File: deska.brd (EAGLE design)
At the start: 72.1 x 55.9 mm, 19 parts, among them Q1 BC547, X1 JST-XH-03-PIN-LONG-PAD, X2 JST-XH-03-PIN-LONG-PAD, X3 JST-XH-03-PIN-LONG-PAD, X4 JST-XH-04-PIN-LONG-PAD, X5 JST-XH-04-PIN-LONG-PAD, X6 JST-XH-04-PIN-LONG-PAD

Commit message: deska
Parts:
- added LED2: (no value), led:LED3MM
- added R7: 220, rcl:0207/7
- moved R5 4.02 mm to (48.3, 34.3), turned to 180 degrees
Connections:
- removed net N$9: WEMOS1.GND, X4.3, X5.3, X6.3
- new net N$4: LED2.A, R7.2
- net +5V: now also R7.1
- net GND: now also LED2.K, WEMOS1.GND, X4.3, X5.3, X6.3
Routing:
- net +5V: track 77.2 -> 138.2 mm
- net N$9: track 25.4 -> 0.00 mm
- net GND: track 166.1 -> 187.7 mm
- net N$4: track 0.00 -> 7.93 mm
- net N$2: track 40.5 -> 43.8 mm
- net N$14: track 29.3 -> 26.7 mm
- net N$7: track 26.9 -> 29.0 mm

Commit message: 0.93
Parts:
- added X7: JST-XH-03-PIN-LONG-PAD, Rembrandt Electronics - JST XH Connectors v1-0:JST-XH-03-PACKAGE-LONG-PAD
- LED2: value (none) -> LED2
- NAPAJENI: value (none) -> 5V
- WEMOS1: value (none) -> WEMOS
- moved R4 10.9 mm to (48.3, 31.8), turned to 180 degrees
- moved R6 10.2 mm to (39.4, 45.7)
- moved LED1 6.35 mm to (35.6, 14.0), turned to 270 degrees
- moved LEDRELAY 6.35 mm to (29.2, 14.0), turned to 270 degrees
- moved R5 2.54 mm to (45.7, 34.3)
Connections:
- removed net N$5: R4.1, WEMOS1.D8
- new net N$9: R3.1, WEMOS1.D7, X3.1
- net +3V3: now also X7.2
- net BUILTINLED: now also R4.1
- net GND: now also X7.1
- net N$1: now also WEMOS1.D5; no longer WEMOS1.D0
- net N$19: now also WEMOS1.D6; no longer WEMOS1.D5
- net N$3: now also WEMOS1.D8, X7.3; no longer R3.1, WEMOS1.D6, X3.1
- net N$8: now also WEMOS1.D0; no longer WEMOS1.D7
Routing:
- net GND: track 187.7 -> 226.2 mm
- net N$2: track 43.8 -> 25.8 mm
- net N$9: track 0.00 -> 14.3 mm
- net +3V3: track 76.6 -> 85.5 mm
- net +5V: track 138.2 -> 130.5 mm
- net N$3: track 16.8 -> 24.0 mm
- net N$7: track 29.0 -> 23.3 mm
- net N$5: track 5.08 -> 0.00 mm
- net BUILTINLED: track 0.00 -> 5.08 mm
- net N$14: track 26.7 -> 30.8 mm
- net N$6: track 16.8 -> 20.2 mm
- net N$8: track 5.08 -> 6.13 mm
- net N$1: track 13.2 -> 14.3 mm, vias 1 -> 0

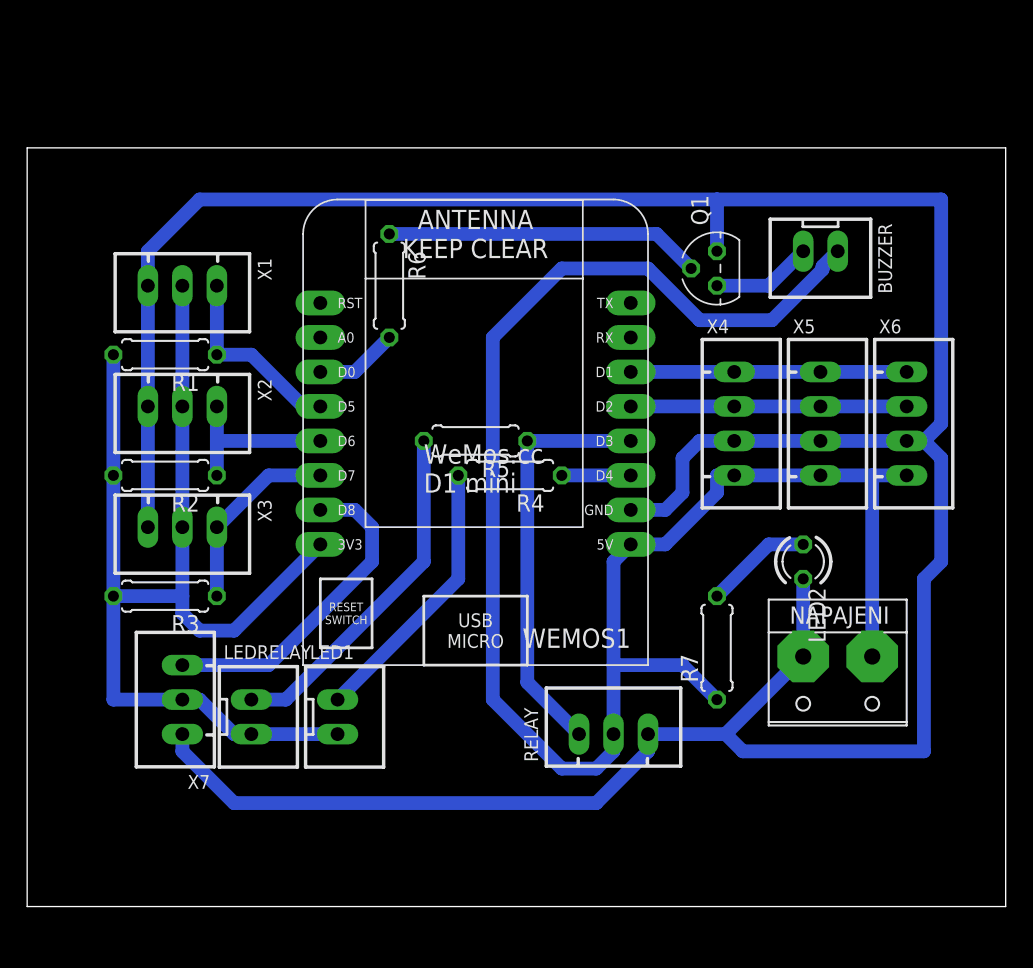
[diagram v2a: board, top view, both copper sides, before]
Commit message: +reset pin na desku +popis pinu
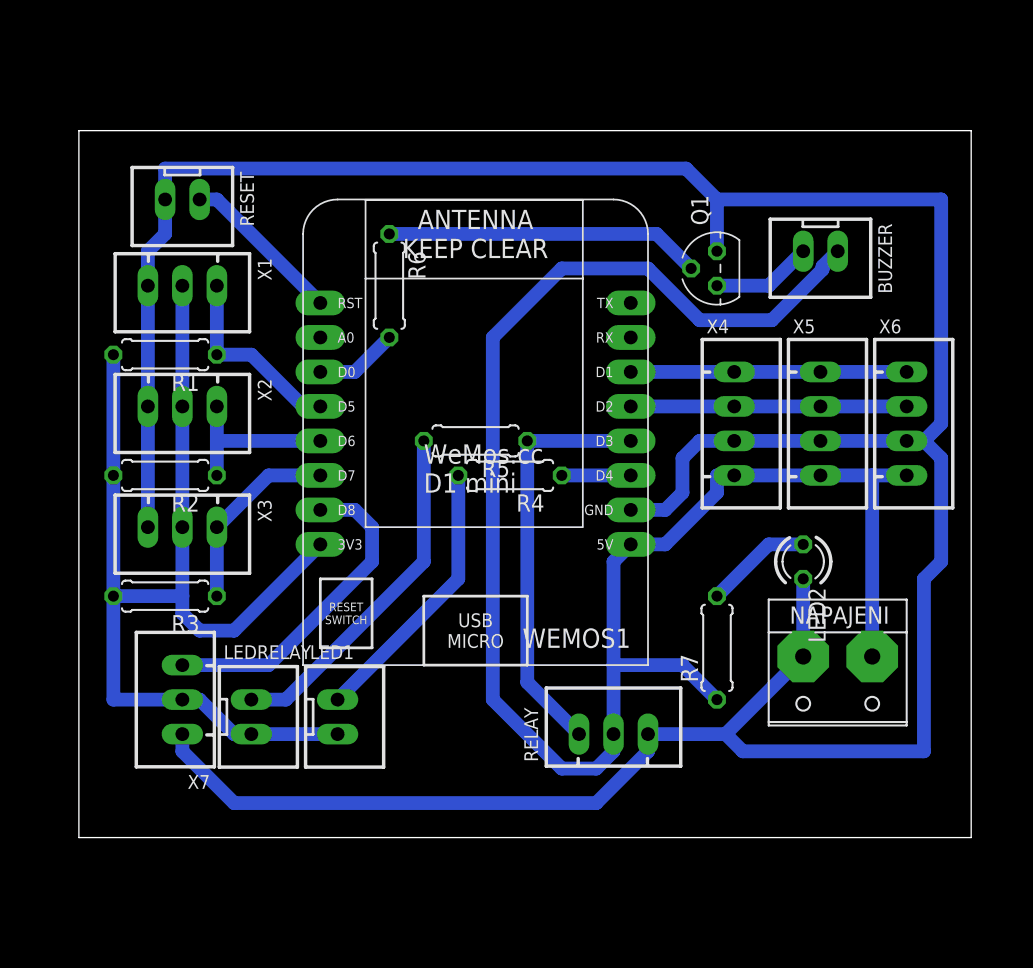
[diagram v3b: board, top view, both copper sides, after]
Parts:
- added RESET: JST-XH-02-PIN-LONG-PAD, Rembrandt Electronics - JST XH Connectors v1-0:JST-XH-02-PACKAGE-LONG-PAD
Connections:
- new net N$5: RESET.1, WEMOS1.RESET
- net GND: now also RESET.2
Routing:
- net N$5: track 0.00 -> 12.0 mm
- net GND: track 226.2 -> 230.9 mm
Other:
- board size 72.1 x 55.9 mm -> 65.7 x 52.1 mm
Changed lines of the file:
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@@
 <board>
 <plain>
-<wire x1="12.7" y1="0" x2="84.76" y2="0" width="0" layer="20"/>
-<wire x1="84.76" y1="0" x2="84.76" y2="55.87" width="0" layer="20"/>
-<wire x1="84.76" y1="55.87" x2="12.7" y2="55.87" width="0" layer="20"/>
-<wire x1="12.7" y1="55.87" x2="12.7" y2="0" width="0" layer="20"/>
+<wire x1="16.51" y1="5.08" x2="82.22" y2="5.08" width="0" layer="20"/>
+<wire x1="82.22" y1="5.08" x2="82.22" y2="57.14" width="0" layer="20"/>
+<wire x1="82.22" y1="57.14" x2="16.51" y2="57.14" width="0" layer="20"/>
+<wire x1="16.51" y1="57.14" x2="16.51" y2="5.08" width="0" layer="20"/>
 </plain>
 <attributes>
@@
 <attribute name="VALUE" x="20.2375" y="10.6375" size="1.016" layer="27" ratio="10" rot="R90"/>
 </element>
+<element name="RESET" library="Rembrandt Electronics - JST XH Connectors v1-0" package="JST-XH-02-PACKAGE-LONG-PAD" value="JST-XH-02-PIN-LONG-PAD" x="24.13" y="52.07" smashed="yes" rot="R180">
+<attribute name="NAME" x="28.385" y="54.11" size="1.016" layer="25" ratio="10" rot="R270"/>
+<attribute name="VALUE" x="27.4325" y="48.1775" size="1.016" layer="27" ratio="10" rot="R180"/>
+</element>
 </elements>
 <signals>
@@
 <contactref element="RELAY" pad="3"/>
 <wire x1="58.42" y1="12.7" x2="64.135" y2="12.7" width="1.016" layer="16"/>
-<wire x1="21.59" y1="48.26" x2="25.4" y2="52.07" width="1.016" layer="16"/>
 <wire x1="21.59" y1="48.26" x2="21.59" y2="45.72" width="1.016" layer="16"/>
 <wire x1="64.135" y1="12.7" x2="69.85" y2="18.415" width="1.016" layer="16"/>
@@
 <wire x1="80.01" y1="52.07" x2="80.01" y2="35.56" width="1.016" layer="16"/>
 <wire x1="80.01" y1="35.56" x2="78.74" y2="34.29" width="1.016" layer="16"/>
-<wire x1="25.4" y1="52.07" x2="63.5" y2="52.07" width="1.016" layer="16"/>
 <wire x1="63.5" y1="52.07" x2="80.01" y2="52.07" width="1.016" layer="16"/>
 <wire x1="63.5" y1="48.26" x2="63.5" y2="52.07" width="1.016" layer="16"/>
@@
 <wire x1="60.96" y1="30.48" x2="60.96" y2="33.02" width="1.016" layer="16"/>
 <wire x1="60.96" y1="33.02" x2="62.23" y2="34.29" width="1.016" layer="16"/>
+<contactref element="RESET" pad="2"/>
+<wire x1="22.86" y1="52.07" x2="22.86" y2="49.53" width="1.016" layer="16"/>
+<wire x1="22.86" y1="49.53" x2="21.59" y2="48.26" width="1.016" layer="16"/>
+<wire x1="22.86" y1="52.07" x2="22.86" y2="54.346" width="1.016" layer="16"/>
+<wire x1="22.86" y1="54.346" x2="61.224" y2="54.346" width="1.016" layer="16"/>
+<wire x1="61.224" y1="54.346" x2="63.5" y2="52.07" width="1.016" layer="16"/>
 </signal>
 <signal name="N$6">
@@
 <wire x1="30.48" y1="17.78" x2="24.13" y2="17.78" width="1.016" layer="16"/>
 </signal>
+<signal name="N$5">
+<contactref element="RESET" pad="1"/>
+<contactref element="WEMOS1" pad="RESET"/>
+<wire x1="25.4" y1="52.07" x2="26.67" y2="52.07" width="1.016" layer="16"/>
+<wire x1="26.67" y1="52.07" x2="34.29" y2="44.45" width="1.016" layer="16"/>
+</signal>
 </signals>

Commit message: +
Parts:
- moved R6 7.73 mm to (38.1, 38.1)
- moved LEDRELAY 3.81 mm to (33.0, 14.0)
- moved X7 3.81 mm to (27.9, 15.2)
- moved LED1 3.81 mm to (39.4, 14.0)
- moved RESET 2.54 mm to (26.7, 52.1)
- moved R7 2.54 mm to (63.5, 21.6)
- moved X5 1.27 mm to (69.8, 35.6)
- moved WEMOS1 1.27 mm to (44.5, 38.1)
- moved R1 1.27 mm to (24.1, 40.6)
- moved R2 1.27 mm to (24.1, 31.8)
- moved R3 1.27 mm to (24.1, 22.9)
- moved X1 1.27 mm to (25.4, 45.7)
- moved X2 1.27 mm to (25.4, 36.8)
- moved X3 1.27 mm to (25.4, 27.9)
- moved X4 1.27 mm to (63.5, 35.6)
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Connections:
- removed net N$3: WEMOS1.D8, X7.3
- new net N$10: WEMOS1.D0, X7.3
- net N$8: now also WEMOS1.D8; no longer WEMOS1.D0
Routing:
- net N$10: track 0.00 -> 32.6 mm
- net N$3: track 24.0 -> 0.00 mm
- net GND: track 230.9 -> 216.0 mm
- net +3V3: track 85.5 -> 90.0 mm
- net N$7: track 23.3 -> 27.7 mm
- net N$5: track 12.0 -> 8.98 mm
- net N$2: track 25.8 -> 22.7 mm
- net N$1: track 14.3 -> 12.5 mm
- net N$6: track 20.2 -> 18.6 mm
- net +5V: track 130.5 -> 128.9 mm
- net N$8: track 6.13 -> 7.62 mm
- net N$19: track 12.7 -> 11.4 mm
- net N$4: track 7.93 -> 6.88 mm
- net N$9: track 14.3 -> 13.5 mm
- net N$12: track 20.3 -> 19.6 mm
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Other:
- board size 65.7 x 52.1 mm -> 70.8 x 67.3 mm

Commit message: +
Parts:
- moved X7 14.2 mm to (41.9, 12.7)
- moved LEDRELAY 7.62 mm to (25.4, 14.0)
- moved LED1 6.35 mm to (33.0, 14.0)
- moved R4 2.84 mm to (47.0, 29.2)
- moved R5 1.27 mm to (45.7, 35.6)
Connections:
- net +3V3: no longer X7.2
- net +5V: now also X7.2
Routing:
- net GND: track 216.0 -> 202.1 mm
- net +5V: track 128.9 -> 136.2 mm
- net N$2: track 22.7 -> 28.6 mm
- net +3V3: track 90.0 -> 85.5 mm
- net N$10: track 32.6 -> 35.5 mm
- net BUILTINLED: track 5.61 -> 7.93 mm
- net N$14: track 31.3 -> 33.1 mm
